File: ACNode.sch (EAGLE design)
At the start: 92 parts, among them IC1 74AHC1G04DCK, IC2 MC78M05CDTG, IC3 LM1117IMP-3.3, IC4 MC78M05CDTG, IC5 ULN2003AN, K1 351, T1 MMBT4401, U2 MAGJACK-POE, U3 CLAMP, Y1 25mhz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

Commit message: First route attempt
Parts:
- added H1, H2, H3, H4: MOUNT-HOLE3.0, holes:MOUNT-HOLE3.0
- added J1: POWER_JACKPTH, SparkFun-Connectors:POWER_JACKPTH
- R11, R16, R17, R18, R4, R5, R6, R7: device SparkFun-Passives:RESISTOR0805-RES -> SparkFun-Passives:RESISTOR0603-RES
- Y2: value 20mhz -> 16mhz
- renumbered X3 to CASE
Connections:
- removed net N$57: SG1.2, SJ11.2
- new net N$23: SG1.2, SJ11.1
- net +3V3: now also SL030.1
- net D3: now also INPUT-2.KL; no longer INPUT-4.KL
- net D4: now also INPUT-3.KL; no longer INPUT-6.KL
- net D5: now also INPUT-4.KL; no longer INPUT-3.KL
- net D6: now also INPUT-5.KL; no longer INPUT-2.KL
- net D7: now also SJ9.1; no longer SJ7.1
- net D9: now also SJ11.2, SJ7.1; no longer SJ11.1, SJ9.1
- net GND: now also INPUT-6.KL, J1.PWR; no longer INPUT-5.KL
- net RAW: now also J1.GND, J1.GNDBREAK
- net SCL: now also R14.1; no longer R14.2
- net VCC: now also R14.2; no longer R14.1, SL030.1
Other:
- moved on the sheet: R14, SJ11

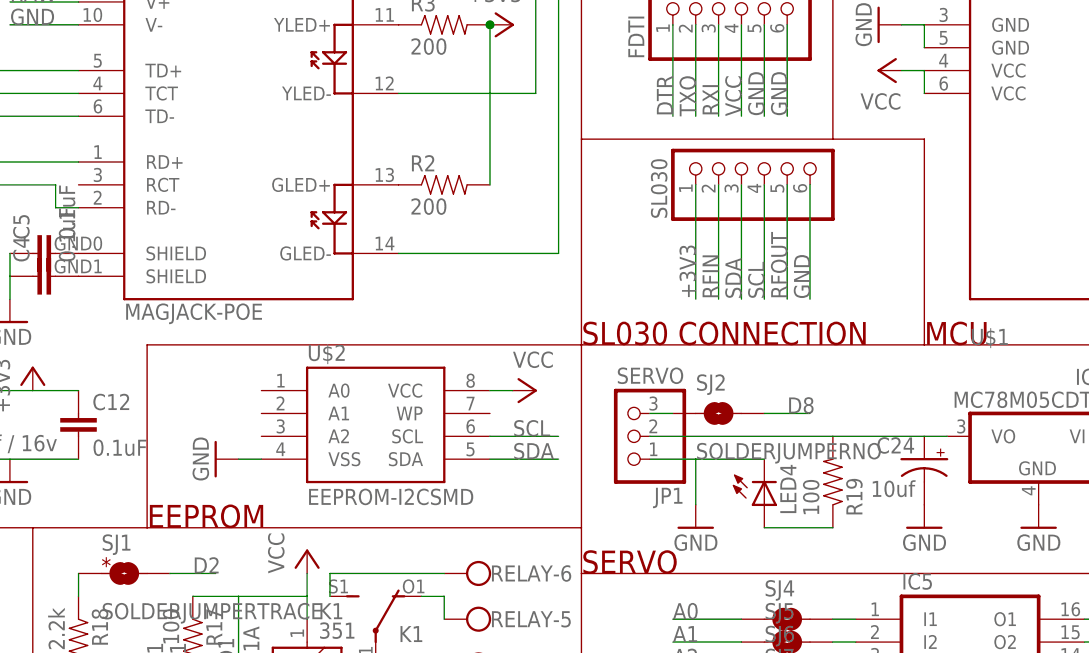
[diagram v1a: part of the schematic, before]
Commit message: Correct SL030 pins
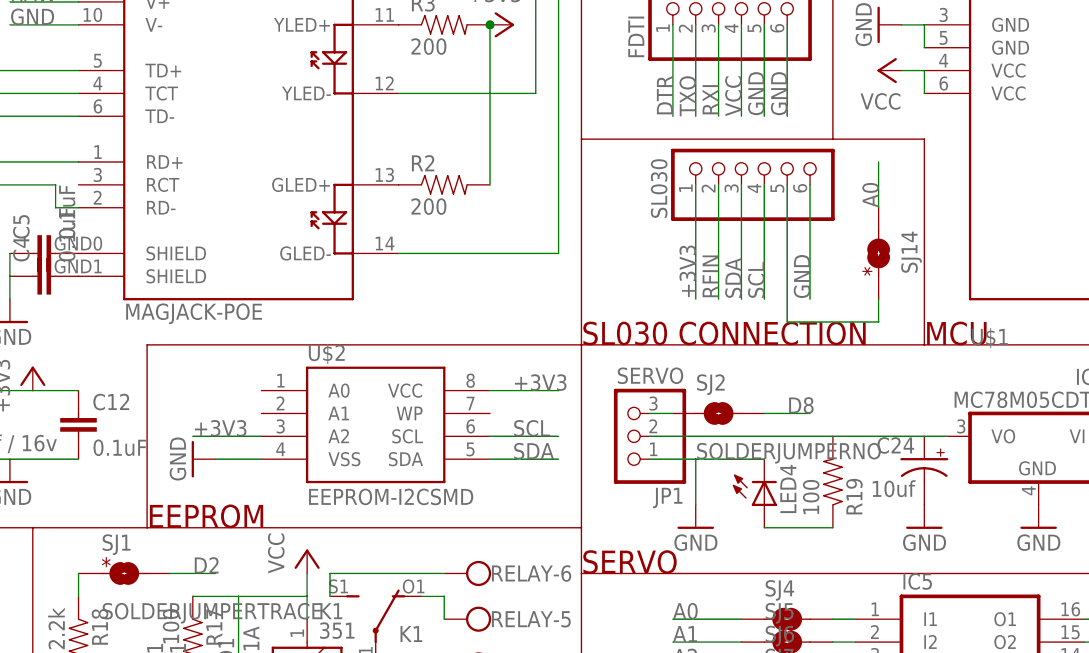
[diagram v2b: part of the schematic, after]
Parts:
- added SJ14: SOLDERJUMPERTRACE, SparkFun-Passives:SOLDERJUMPERTRACE
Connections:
- removed net RFOUT: SL030.5
- new net N$57: SJ14.2, SL030.5
- net +3V3: now also U$2.A2, U$2.VCC
- net A0: now also SJ14.1
- net VCC: no longer U$2.VCC
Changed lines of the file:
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@@
 <part name="GND16" library="supply1" deviceset="GND" device=""/>
 <part name="U$2" library="SparkFun-DigitalIC" deviceset="EEPROM-I2C" device="SMD"/>
-<part name="P+4" library="supply1" deviceset="VCC" device=""/>
 <part name="GND17" library="supply1" deviceset="GND" device=""/>
 <part name="R13" library="SparkFun-Passives" deviceset="RESISTOR" device="0603-RES" value="4.7k"/>
@@
 <part name="H4" library="holes" deviceset="MOUNT-HOLE" device="3.0"/>
 <part name="J1" library="SparkFun-Connectors" deviceset="POWER_JACK" device="PTH"/>
+<part name="SJ14" library="SparkFun-Passives" deviceset="SOLDERJUMPER" device="TRACE" value=""/>
 </parts>
 <sheets>
@@
 <text x="91.44" y="45.72" size="1.778" layer="94">*</text>
 <wire x1="261.62" y1="93.98" x2="261.62" y2="35.56" width="0.1524" layer="94"/>
+<text x="195.58" y="101.6" size="1.778" layer="94" rot="R90">*</text>
 </plain>
 <instances>
@@
 <instance part="GND16" gate="1" x="185.42" y="139.7" rot="R270"/>
 <instance part="U$2" gate="G$1" x="139.7" y="83.82"/>
-<instance part="P+4" gate="VCC" x="157.48" y="88.9" rot="R270"/>
-<instance part="GND17" gate="1" x="121.92" y="81.28" rot="R270"/>
+<instance part="GND17" gate="1" x="119.38" y="81.28" rot="R270"/>
 <instance part="R13" gate="G$1" x="223.52" y="154.94" rot="R90"/>
 <instance part="R14" gate="G$1" x="215.9" y="167.64" rot="R90"/>
@@
 <instance part="H4" gate="G$1" x="50.8" y="170.18"/>
 <instance part="J1" gate="G$1" x="15.24" y="63.5" rot="R90"/>
+<instance part="SJ14" gate="1" x="195.58" y="104.14" rot="R270"/>
 </instances>
 <busses>
@@
 <pinref part="GND17" gate="1" pin="GND"/>
 <pinref part="U$2" gate="G$1" pin="VSS"/>
-<wire x1="124.46" y1="81.28" x2="127" y2="81.28" width="0.1524" layer="91"/>
+<wire x1="121.92" y1="81.28" x2="127" y2="81.28" width="0.1524" layer="91"/>
 </segment>
 <segment>
@@
 <label x="175.26" y="99.06" size="1.778" layer="95" rot="R90"/>
 </segment>
+<segment>
+<pinref part="U$2" gate="G$1" pin="VCC"/>
+<wire x1="152.4" y1="88.9" x2="160.02" y2="88.9" width="0.1524" layer="91"/>
+<label x="154.94" y="88.9" size="1.778" layer="95"/>
+</segment>
+<segment>
+<pinref part="U$2" gate="G$1" pin="A2"/>
+<wire x1="127" y1="83.82" x2="119.38" y2="83.82" width="0.1524" layer="91"/>
+<label x="119.38" y="83.82" size="1.778" layer="95"/>
+</segment>
 </net>
 <net name="N$9" class="0">
@@
 </segment>
 <segment>
-<pinref part="U$2" gate="G$1" pin="VCC"/>
-<pinref part="P+4" gate="VCC" pin="VCC"/>
-<wire x1="152.4" y1="88.9" x2="154.94" y2="88.9" width="0.1524" layer="91"/>
-</segment>
-<segment>
 <pinref part="R13" gate="G$1" pin="2"/>
 <pinref part="P+5" gate="VCC" pin="VCC"/>
@@
 </segment>
 </net>
-<net name="RFOUT" class="0">
-<segment>
-<pinref part="SL030" gate="A" pin="5"/>
-<wire x1="185.42" y1="111.76" x2="185.42" y2="99.06" width="0.1524" layer="91"/>
-<label x="185.42" y="99.06" size="1.778" layer="95" rot="R90"/>
-</segment>
-</net>
 <net name="RAW" class="0">
 <segment>
@@
 <wire x1="180.34" y1="63.5" x2="172.72" y2="63.5" width="0.1524" layer="91"/>
 <label x="172.72" y="63.5" size="1.778" layer="95"/>
+</segment>
+<segment>
+<pinref part="SJ14" gate="1" pin="1"/>
+<wire x1="195.58" y1="109.22" x2="195.58" y2="114.3" width="0.1524" layer="91"/>
+<label x="195.58" y="109.22" size="1.778" layer="95" rot="R90"/>
 </segment>
 </net>
@@
 </segment>
 </net>
+<net name="N$57" class="0">
+<segment>
+<pinref part="SL030" gate="A" pin="5"/>
+<wire x1="185.42" y1="111.76" x2="185.42" y2="96.52" width="0.1524" layer="91"/>
+<pinref part="SJ14" gate="1" pin="2"/>
+<wire x1="185.42" y1="96.52" x2="195.58" y2="96.52" width="0.1524" layer="91"/>
+<wire x1="195.58" y1="96.52" x2="195.58" y2="99.06" width="0.1524" layer="91"/>
+</segment>
+</net>
